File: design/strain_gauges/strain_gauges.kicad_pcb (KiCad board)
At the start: 2 copper layers, 106.7 x 52.7 mm, 36 parts, among them J1 Conn_01x03, J2 Conn_01x03, J3 Conn_01x08, J4 Conn_01x04_swapped, J5 Conn_01x04_swapped, J6 Conn_01x04_swapped, J7 Conn_01x04_swapped, P1 CONN_01X02, Q1 BC640, U1 LT1460-10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

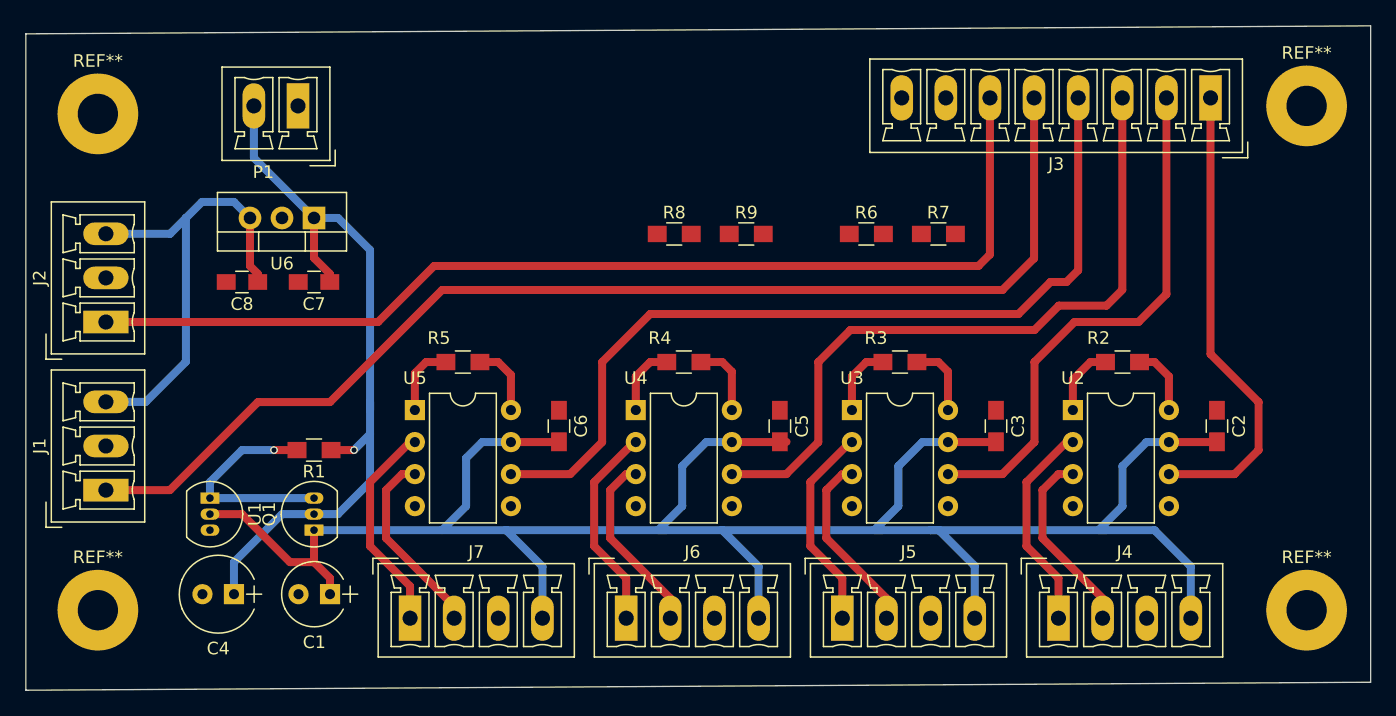
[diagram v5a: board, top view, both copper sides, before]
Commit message: Board layout & routing rework
- Move the power blocks further into the board
- ground planing not done yet
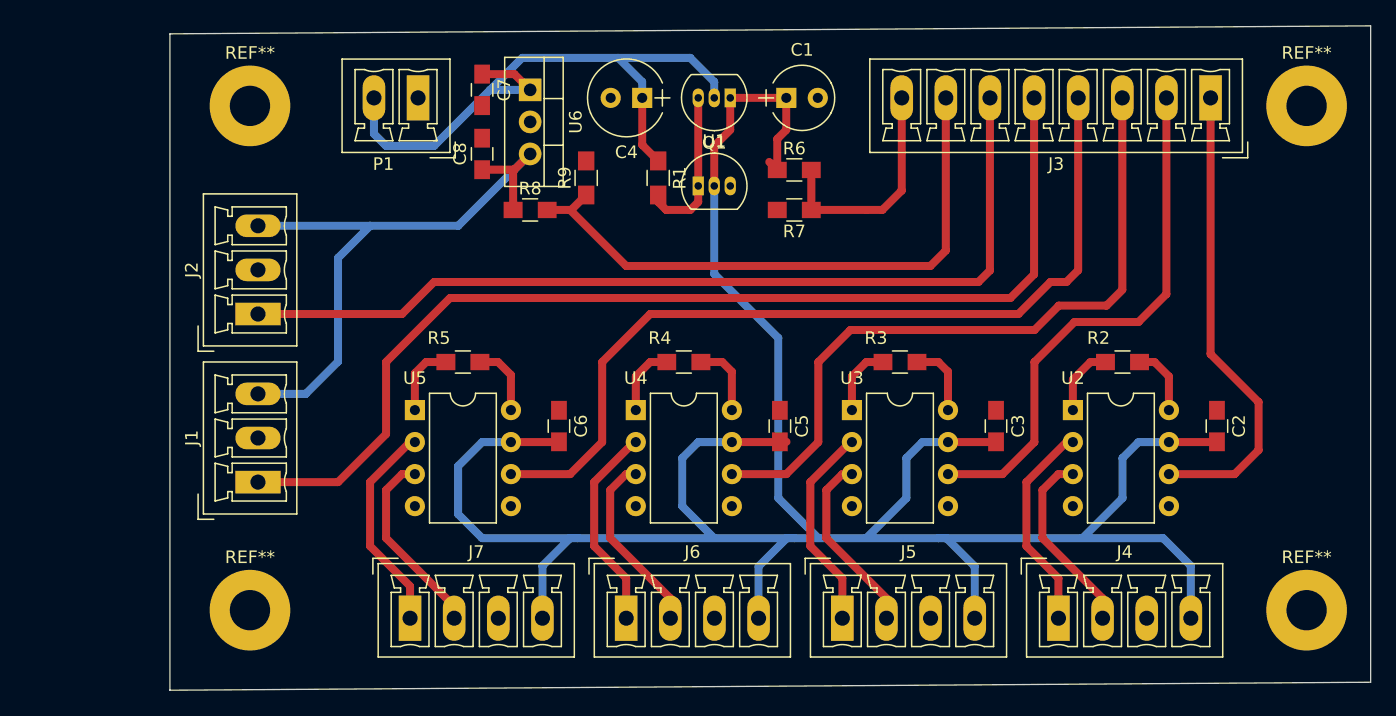
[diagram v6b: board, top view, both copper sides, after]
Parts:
- moved C1 53.5 mm to (130.4, 117.4), turned to 0 degrees
- moved C4 51.0 mm to (119.0, 117.4)
- moved Q1 47.6 mm to (126.0, 117.4), turned to 180 degrees
- moved U1 46.0 mm to (123.4, 124.4), turned to 0 degrees
- moved R1 34.8 mm to (120.2, 123.8), turned to 270 degrees
- moved C8 21.6 mm to (106.3, 121.9), turned to 90 degrees
- moved C7 20.3 mm to (106.3, 116.8), turned to 270 degrees
- moved U6 19.9 mm to (110.1, 116.8), turned to 270 degrees
- moved R9 13.5 mm to (114.5, 123.8), turned to 90 degrees
- moved J1 12.1 mm to (88.5, 147.9)
- moved J2 12.1 mm to (88.5, 134.6)
- moved REF** 12.1 mm to (87.9, 118.1)
- moved REF** 12.1 mm to (87.9, 158.1)
- moved R7 11.6 mm to (131.0, 126.3), turned to 180 degrees
- moved R8 11.6 mm to (110.1, 126.3)
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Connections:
- R6 pad 2: Net-(J3-Pad7) -> Net-(J3-Pad8)
- R7 pad 1: Net-(J3-Pad7) -> Net-(J3-Pad8)
- R8 pad 2: Net-(J3-Pad8) -> Net-(J3-Pad7)
- R9 pad 1: Net-(J3-Pad8) -> Net-(J3-Pad7)
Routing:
- net Net-(J3-Pad7): track 0.00 -> 47.8 mm
- net +10V: track 175.3 -> 197.7 mm
- net Net-(J3-Pad8): track 0.00 -> 18.3 mm
- net +15V: track 37.4 -> 50.8 mm
- net PRESSURE_2: track 84.8 -> 73.2 mm
- net +16V: track 60.6 -> 52.2 mm, vias 1 -> 0
- net PRESSURE_1: track 94.0 -> 85.7 mm
- net Net-(Q1-Pad3): track 18.1 -> 12.5 mm, vias 1 -> 0
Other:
- board size 106.7 x 52.7 mm -> 95.2 x 52.7 mm

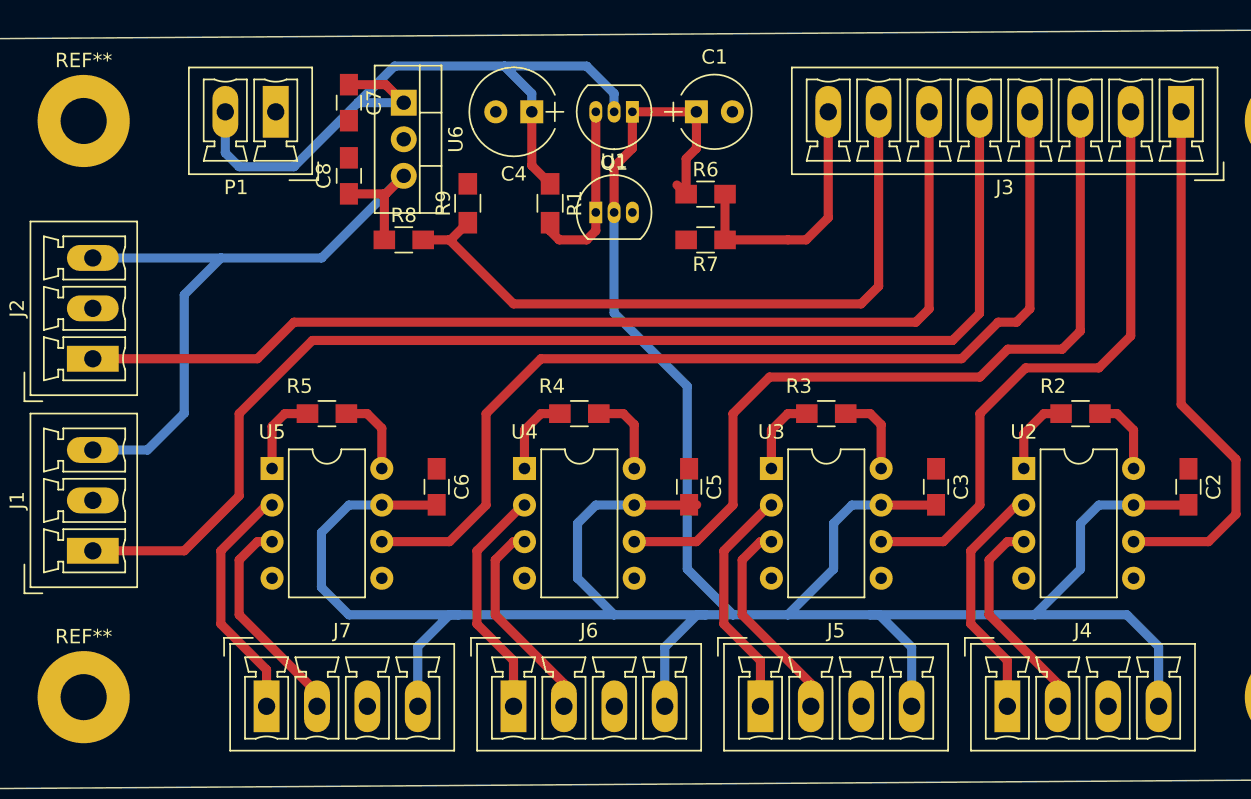
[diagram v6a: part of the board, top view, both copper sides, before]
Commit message: Make power traces fatter
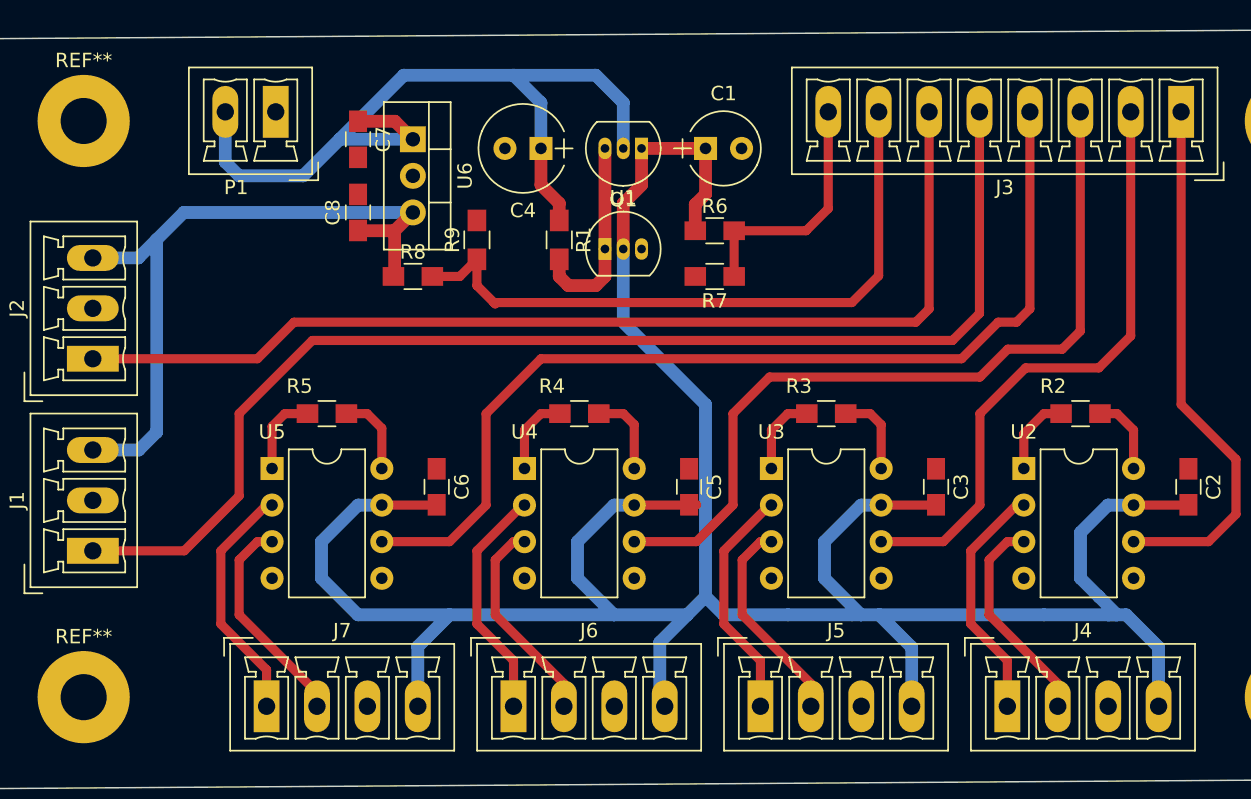
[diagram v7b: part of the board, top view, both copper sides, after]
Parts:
- moved C4 2.62 mm to (119.6, 120.0)
- moved C8 2.62 mm to (106.9, 124.4)
- moved Q1 2.62 mm to (126.6, 120.0)
- moved R8 2.62 mm to (110.7, 128.9)
- moved C1 2.62 mm to (131.0, 120.0)
- moved R6 2.62 mm to (131.7, 125.7)
- moved R7 2.62 mm to (131.7, 128.9)
- moved C7 2.62 mm to (106.9, 119.3)
- moved R1 2.62 mm to (120.9, 126.3)
- moved U6 2.62 mm to (110.7, 119.3)
- moved R9 2.62 mm to (115.2, 126.3)
- moved U1 2.62 mm to (124.0, 127.0)
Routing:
- net +10V: track 197.7 -> 189.3 mm
- net +16V: track 52.2 -> 59.2 mm
- net Net-(Q1-Pad3): track 12.5 -> 14.3 mm
- net Net-(J3-Pad7): track 47.8 -> 46.2 mm
- net +15V: track 50.8 -> 49.4 mm
- net Net-(J3-Pad8): track 18.3 -> 17.1 mm

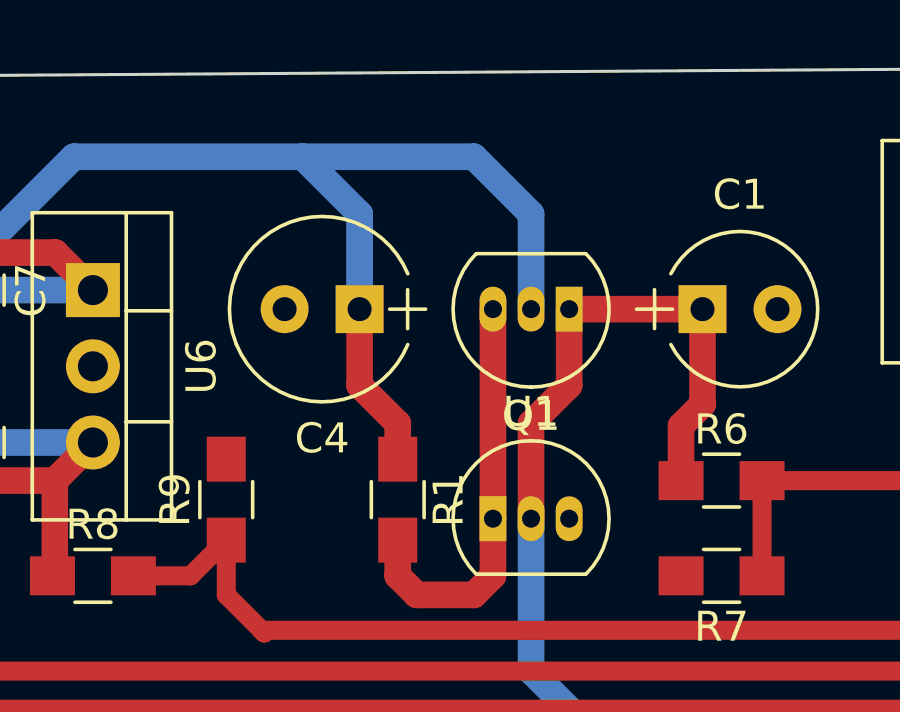
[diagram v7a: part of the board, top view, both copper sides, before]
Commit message: Correct PNP orientation in schematic
Also swap out the part for one I have on hand (2N3906)
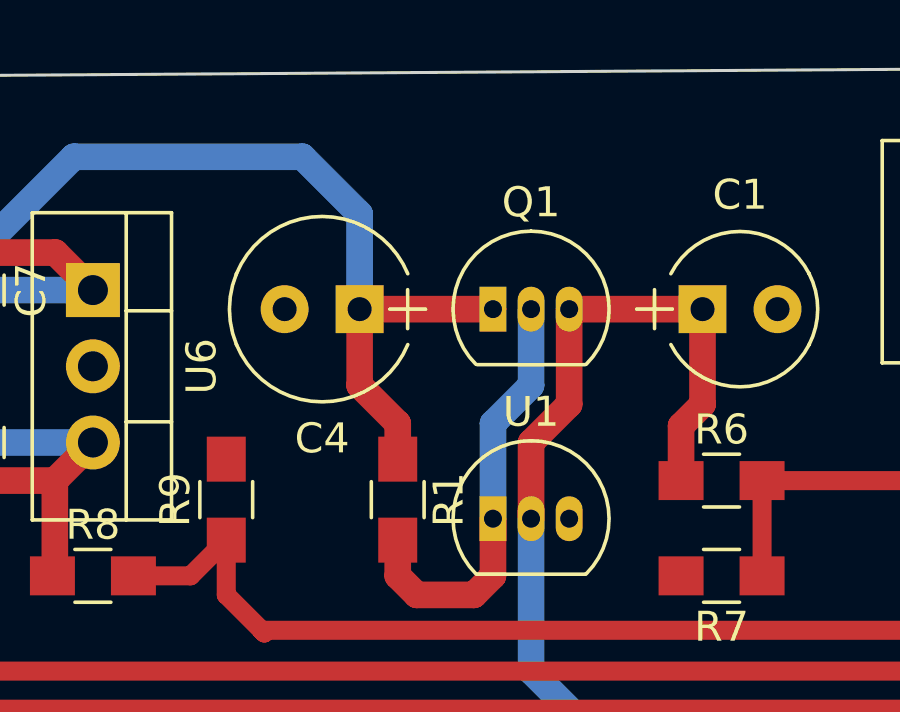
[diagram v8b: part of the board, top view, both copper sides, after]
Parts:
- Q1: value BC640 -> 2N3096
- moved Q1 2.54 mm to (124.0, 120.0), turned to 0 degrees
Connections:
- Q1 pad 1: +10V -> +16V
- Q1 pad 2: +16V -> Net-(Q1-Pad2)
- Q1 pad 3: Net-(Q1-Pad3) -> +10V
- R1 pad 2: Net-(Q1-Pad3) -> Net-(Q1-Pad2)
- U1 pad 1: Net-(Q1-Pad3) -> Net-(Q1-Pad2)
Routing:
- net Net-(Q1-Pad2): track 0.00 -> 14.9 mm
- net Net-(Q1-Pad3): track 14.3 -> 0.00 mm
- net +16V: track 59.2 -> 52.0 mm
